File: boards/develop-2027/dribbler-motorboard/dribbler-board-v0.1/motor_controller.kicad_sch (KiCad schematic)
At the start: 27 parts, among them SW1 RESET, U1 STSPIN32G0A2

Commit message: Shunt resistor power consumption validated
Validated shunt resistor max power consumption does not exceed 3W limit
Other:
- note added: "Shunt Resistor Power Consumption P = (0.015 Ohms) * (11.01A)^2 = 1.818 W"
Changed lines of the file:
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@@
+		)
+	)
+	(text "Shunt Resistor Power Consumption\nP = (0.015 Ohms) * (11.01A)^2 = 1.818 W"
+		(exclude_from_sim no)
+		(at 129.286 139.446 0)
+		(effects
+			(font
+				(size 1.27 1.27)
+				(color 0 0 194 1)
+			)
 		)
 	)

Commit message: updated overcurrent resistors
updated part numbers for overcurrent circuit resistors
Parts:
- R14: Vendor P/N YAG1412CT-ND -> YAG1370CT-ND
- R15: Vendor P/N YAG1370CT-ND -> YAG1412CT-ND
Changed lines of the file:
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@@
 	(wire
 		(pts
-			(xy 60.96 30.48) (xy 60.96 31.75)
-		)
-		(stroke
-			(width 0)
-			(type default)
-		)
-	)
-	(wire
-		(pts
 			(xy 147.32 118.11) (xy 149.86 118.11)
 		)
@@
 			)
 		)
-		(property "Vendor P/N" "YAG1412CT-ND"
+		(property "Vendor P/N" "YAG1370CT-ND"
 			(at 222.25 114.3 0)
 			(hide yes)
@@
 			)
 		)
-		(property "Vendor P/N" "YAG1370CT-ND"
+		(property "Vendor P/N" "YAG1412CT-ND"
 			(at 209.55 120.65 0)
 			(hide yes)

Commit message: Updated passives part numbers
Updated resistors with digikey part numbers
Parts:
- R48: Vendor (none) -> DigiKey; Vendor P/N (none) -> RMCF0402FT10K0CT-ND
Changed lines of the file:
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@@
 			)
 		)
-		(property "Vendor" ""
+		(property "Vendor" "DigiKey"
 			(at 152.4 35.56 0)
 			(hide yes)
@@
 			)
 		)
-		(property "Vendor P/N" ""
+		(property "Vendor P/N" "RMCF0402FT10K0CT-ND"
 			(at 152.4 35.56 0)
 			(hide yes)

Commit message: Updated for BOM consolidation
Updated component references and part numbers for BOM consolidation
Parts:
- removed C7: 100n 10V, Capacitor_SMD:C_0402_1005Metric, symbol Device:C
- added C5: 1u 63V, Capacitor_SMD:C_0603_1608Metric, symbol Device:C
- C6: value 1u 10V -> 100n 25V; Manufacturer P/N GRM155R61E105KA12D -> CL05A104KA5NNNC; Vendor P/N 490-10017-1-ND -> 1276-1043-1-ND
- R5: renamed from R48; Vendor P/N RMCF0402FT10K0CT-ND -> 311-10KJRCT-ND
- renumbered C11 to C10, C12 to C11, C13 to C12, C3 to C2, C4 to C3, C5 to C4, C8 to C7, C9 to C8, C10 to C9, R12 to R6, R50 to R7, R14 to R8, R15 to R9, TP6 to TP2, TP7 to TP3, TP8 to TP4, TP9 to TP5, TP10 to TP6, TP11 to TP7, TP12 to TP8, TP13 to TP9
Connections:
- net +3.3V: now also C5.1
- net GND: now also C5.2

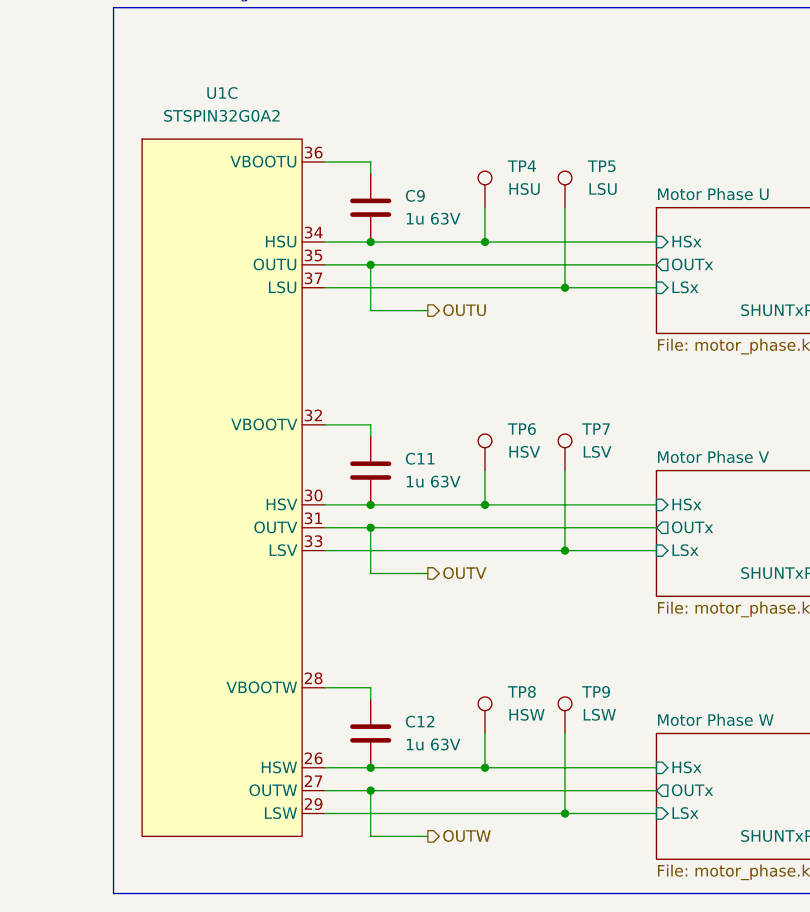
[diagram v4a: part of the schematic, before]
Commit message: bootstrap capacitor fix
bootstrap capacitor moved to correct OUTU/OUTx line instead of HSU/HSx
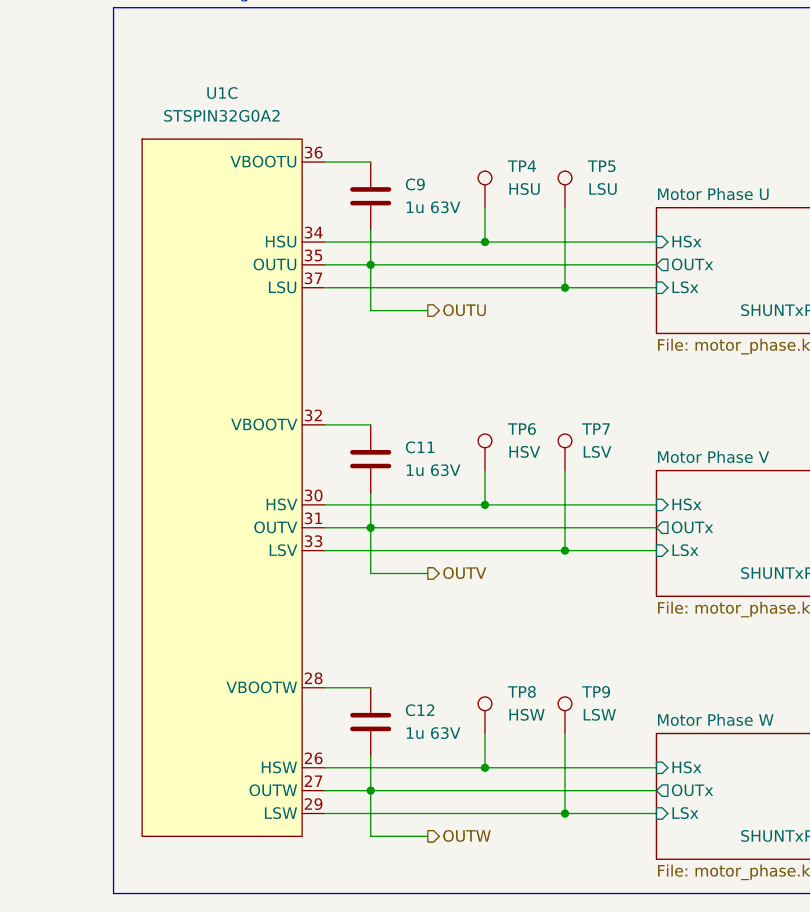
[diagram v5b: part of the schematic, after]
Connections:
- net Motor Phase U/HSx: no longer C9.2
- net Motor Phase V/HSx: no longer C11.2
- net Motor Phase W/HSx: no longer C12.2
- net OUTU: now also C9.2
- net OUTV: now also C11.2
- net OUTW: now also C12.2
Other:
- moved on the sheet: C11, C12, C9
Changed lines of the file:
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@@
 	)
 	(junction
-		(at 44.45 182.88)
-		(diameter 0)
-		(color 0 0 0 0)
-	)
-	(junction
 		(at 107.95 73.66)
 		(diameter 0)
@@
 	)
 	(junction
-		(at 44.45 153.67)
-		(diameter 0)
-		(color 0 0 0 0)
-	)
-	(junction
 		(at 36.83 55.88)
 		(diameter 0)
@@
 	)
 	(junction
-		(at 44.45 124.46)
-		(diameter 0)
-		(color 0 0 0 0)
-	)
-	(junction
 		(at 105.41 161.29)
 		(diameter 0)
@@
 	(wire
 		(pts
-			(xy 44.45 144.78) (xy 44.45 146.05)
-		)
-		(stroke
-			(width 0)
-			(type default)
-		)
-	)
-	(wire
-		(pts
 			(xy 66.04 120.65) (xy 66.04 129.54)
 		)
@@
 	(wire
 		(pts
-			(xy 39.37 182.88) (xy 44.45 182.88)
-		)
-		(stroke
-			(width 0)
-			(type default)
-		)
-	)
-	(wire
-		(pts
 			(xy 231.14 48.26) (xy 247.65 48.26)
 		)
@@
 	(wire
 		(pts
+			(xy 44.45 123.19) (xy 44.45 127)
+		)
+		(stroke
+			(width 0)
+			(type default)
+		)
+	)
+	(wire
+		(pts
 			(xy 172.72 185.42) (xy 171.45 185.42)
 		)
@@
 	(wire
 		(pts
-			(xy 44.45 182.88) (xy 57.15 182.88)
+			(xy 39.37 182.88) (xy 57.15 182.88)
 		)
 		(stroke
@@
 	(wire
 		(pts
-			(xy 44.45 115.57) (xy 44.45 116.84)
-		)
-		(stroke
-			(width 0)
-			(type default)
-		)
-	)
-	(wire
-		(pts
 			(xy 50.8 161.29) (xy 44.45 161.29)
 		)
@@
 	(wire
 		(pts
-			(xy 44.45 173.99) (xy 44.45 175.26)
+			(xy 44.45 181.61) (xy 44.45 185.42)
 		)
 		(stroke
@@
 		)
 	)
+	(wire
+		(pts
+			(xy 44.45 152.4) (xy 44.45 156.21)
+		)
+		(stroke
+			(width 0)
+			(type default)
+		)
+	)
 	(bus
 		(pts
@@
 	(wire
 		(pts
-			(xy 39.37 153.67) (xy 44.45 153.67)
-		)
-		(stroke
-			(width 0)
-			(type default)
-		)
-	)
-	(wire
-		(pts
-			(xy 44.45 153.67) (xy 57.15 153.67)
+			(xy 39.37 153.67) (xy 57.15 153.67)
 		)
 		(stroke
@@
 	(wire
 		(pts
-			(xy 39.37 124.46) (xy 44.45 124.46)
+			(xy 39.37 124.46) (xy 57.15 124.46)
 		)
 		(stroke
@@
 	(wire
 		(pts
-			(xy 44.45 124.46) (xy 57.15 124.46)
-		)
-		(stroke
-			(width 0)
-			(type default)
-		)
-	)
-	(wire
-		(pts
 			(xy 149.86 40.64) (xy 152.4 40.64)
 		)
@@
 	(symbol
 		(lib_id "Device:C")
-		(at 44.45 179.07 0)
+		(at 44.45 177.8 0)
 		(unit 1)
 		(body_style 1)
@@
 		(fields_autoplaced yes)
 		(property "Reference" "C12"
-			(at 48.26 177.7999 0)
+			(at 48.26 176.5299 0)
 			(show_name no)
 			(do_not_autoplace no)
@@
 		)
 		(property "Value" "1u 63V"
-			(at 48.26 180.3399 0)
+			(at 48.26 179.0699 0)
 			(show_name no)
 			(do_not_autoplace no)
@@
 		)
 		(property "Footprint" "Capacitor_SMD:C_0603_1608Metric"
-			(at 45.4152 182.88 0)
+			(at 45.4152 181.61 0)
 			(hide yes)
 			(show_name no)
@@
 		)
 		(property "Datasheet" "https://search.murata.co.jp/Ceramy/image/img/A01X/G101/ENG/GRM188D72A105KE01-01A.pdf"
-			(at 44.45 179.07 0)
+			(at 44.45 177.8 0)
 			(hide yes)
 			(show_name no)
@@
 		)
 		(property "Description" "Unpolarized capacitor"
-			(at 44.45 179.07 0)
+			(at 44.45 177.8 0)
 			(hide yes)
 			(show_name no)
@@
 		)
 		(property "Manufacturer P/N" "GRM188D72A105KE01J"
-			(at 44.45 179.07 0)
+			(at 44.45 177.8 0)
 			(hide yes)
 			(show_name no)
@@
 		)
 		(property "Vendor" "DigiKey"
-			(at 44.45 179.07 0)
+			(at 44.45 177.8 0)
 			(hide yes)
 			(show_name no)
@@
 		)
 		(property "Vendor P/N" "490-GRM188D72A105KE01JCT-ND"
-			(at 44.45 179.07 0)
+			(at 44.45 177.8 0)
 			(hide yes)
 			(show_name no)
@@
 	(symbol
 		(lib_id "Device:C")
-		(at 44.45 149.86 0)
+		(at 44.45 148.59 0)
 		(unit 1)
 		(body_style 1)
@@
 		(fields_autoplaced yes)
 		(property "Reference" "C11"
-			(at 48.26 148.5899 0)
+			(at 48.26 147.3199 0)
 			(show_name no)
 			(do_not_autoplace no)
@@
 		)
 		(property "Value" "1u 63V"
-			(at 48.26 151.1299 0)
+			(at 48.26 149.8599 0)
 			(show_name no)
 			(do_not_autoplace no)
@@
 		)
 		(property "Footprint" "Capacitor_SMD:C_0603_1608Metric"
-			(at 45.4152 153.67 0)
+			(at 45.4152 152.4 0)
 			(hide yes)
 			(show_name no)
@@
 		)
 		(property "Datasheet" "https://search.murata.co.jp/Ceramy/image/img/A01X/G101/ENG/GRM188D72A105KE01-01A.pdf"
-			(at 44.45 149.86 0)
+			(at 44.45 148.59 0)
 			(hide yes)
 			(show_name no)
@@
 		)
 		(property "Description" "Unpolarized capacitor"
-			(at 44.45 149.86 0)
+			(at 44.45 148.59 0)
 			(hide yes)
 			(show_name no)
@@
 		)
 		(property "Manufacturer P/N" "GRM188D72A105KE01J"
-			(at 44.45 149.86 0)
+			(at 44.45 148.59 0)
 			(hide yes)
 			(show_name no)
@@
 		)
 		(property "Vendor" "DigiKey"
-			(at 44.45 149.86 0)
+			(at 44.45 148.59 0)
 			(hide yes)
 			(show_name no)
@@
 		)
 		(property "Vendor P/N" "490-GRM188D72A105KE01JCT-ND"
-			(at 44.45 149.86 0)
+			(at 44.45 148.59 0)
 			(hide yes)
 			(show_name no)
@@
 	(symbol
 		(lib_id "Device:C")
-		(at 44.45 120.65 0)
+		(at 44.45 119.38 0)
 		(unit 1)
 		(body_style 1)
@@
 		(fields_autoplaced yes)
 		(property "Reference" "C9"
-			(at 48.26 119.3799 0)
+			(at 48.26 118.1099 0)
 			(show_name no)
 			(do_not_autoplace no)
@@
 		)
 		(property "Value" "1u 63V"
-			(at 48.26 121.9199 0)
+			(at 48.26 120.6499 0)
 			(show_name no)
 			(do_not_autoplace no)
@@
 		)
 		(property "Footprint" "Capacitor_SMD:C_0603_1608Metric"
-			(at 45.4152 124.46 0)
+			(at 45.4152 123.19 0)
 			(hide yes)
 			(show_name no)
@@
 		)
 		(property "Datasheet" "https://search.murata.co.jp/Ceramy/image/img/A01X/G101/ENG/GRM188D72A105KE01-01A.pdf"
-			(at 44.45 120.65 0)
+			(at 44.45 119.38 0)
 			(hide yes)
 			(show_name no)
@@
 		)
 		(property "Description" "Unpolarized capacitor"
-			(at 44.45 120.65 0)
+			(at 44.45 119.38 0)
 			(hide yes)
 			(show_name no)
@@
 		)
 		(property "Manufacturer P/N" "GRM188D72A105KE01J"
-			(at 44.45 120.65 0)
+			(at 44.45 119.38 0)
 			(hide yes)
 			(show_name no)
@@
 		)
 		(property "Vendor" "DigiKey"
-			(at 44.45 120.65 0)
+			(at 44.45 119.38 0)
 			(hide yes)
 			(show_name no)
@@
 		)
 		(property "Vendor P/N" "490-GRM188D72A105KE01JCT-ND"
-			(at 44.45 120.65 0)
+			(at 44.45 119.38 0)
 			(hide yes)
 			(show_name no)

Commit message: updated for b2
aiden pls review
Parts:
- removed U1: STSPIN32G0A2, Package_DFN_QFN:VQFN-48-1EP_7x7mm_P0.5mm_EP2.6x2.6mm, symbol RJ-MCU:STSPIN32G0A2
- added U4: STSPIN32G0B2, Package_DFN_QFN:VQFN-48-1EP_7x7mm_P0.5mm_EP2.6x2.6mm, symbol RJ-MCU:STSPIN32G0B2
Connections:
- net +3.3V: now also U4.38 (~{STBY}), U4.5 (VDD), U4.9 (REG3V3)
- net Current Sensing/OPxN: now also U4.23 (OP1N)
- net Current Sensing/OPxO: now also U4.22 (OP1O)
- net Current Sensing/OPxP: now also U4.24 (OP1P)
- net FAULT: now also U4.1 (PC13)
- net GND: now also U4.19 (TESTMODE), U4.44 (GND), U4.49 (EPAD)
- net HALL.A: now also U4.12 (PA0/TIM2_CH1)
- net HALL.B: now also U4.13 (PA1/TIM2_CH2)
- net HALL.C: now also U4.14 (PA2/TIM2_CH3)
- net I2C.SCL: now also U4.45 (PB6/I2C1_SCL)
- net I2C.SDA: now also U4.46 (PB7/I2C1_SDA)
- net I_{SENSE}: now also U4.21 (PB1/ADC_IN)
- net Motor Phase U/HSx: now also U4.34 (HSU)
- net Motor Phase U/LSx: now also U4.37 (LSU)
- net Motor Phase V/HSx: now also U4.30 (HSV)
- net Motor Phase V/LSx: now also U4.33 (LSV)
- net Motor Phase W/HSx: now also U4.26 (HSW)
- net Motor Phase W/LSx: now also U4.29 (LSW)
- net OUTU: now also U4.35 (OUTU)
- net OUTV: now also U4.31 (OUTV)
- net OUTW: now also U4.27 (OUTW)
- net SPI.CSN: now also U4.16 (PA4/SPI1_~{SS})
- net SPI.MISO: now also U4.18 (PA6/SPI1_MISO)
- net SPI.MOSI: now also U4.20 (PA7/SPI1_MOSI)
- net SPI.SCK: now also U4.17 (PA5/SPI1_SCK)
- net SWD.CLK: now also U4.40 (PA13/SWCLK)
- net SWD.IO: now also U4.41 (PA14/SWDIO/BOOT0)
- net TEMP_SENSE: now also U4.39 (PA12[PA10]/SPI2_MOSI)
- net VBUS: now also U4.7 (VM)
- net ~{RST}: now also U4.11 (PF2/~{RST})
- net at C12.1: now also U4.28 (VBOOTW)
- net at C10.1, R8.1, R9.2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: now also U4.25 (OCCOMP)
- net at C7.1, C8.1, TP2.1: now also U4.6 (REG12)
- net at C11.1: now also U4.32 (VBOOTV)
- net at C9.1: now also U4.36 (VBOOTU)
- no-connect marks 4 -> 10
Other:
- note removed: "Unused"
- moved on the sheet: D3, R5, R6, SW1
